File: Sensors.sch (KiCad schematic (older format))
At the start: 50 parts, among them CON1 CONSOLE, P1 CONN_02X20, P10 CBUS, P11 I2C0, P12 I2C0, P13 I2C1, P14 I2C1, P7 96B_SPI, Q2 CJ2305, Q3 CJ2305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

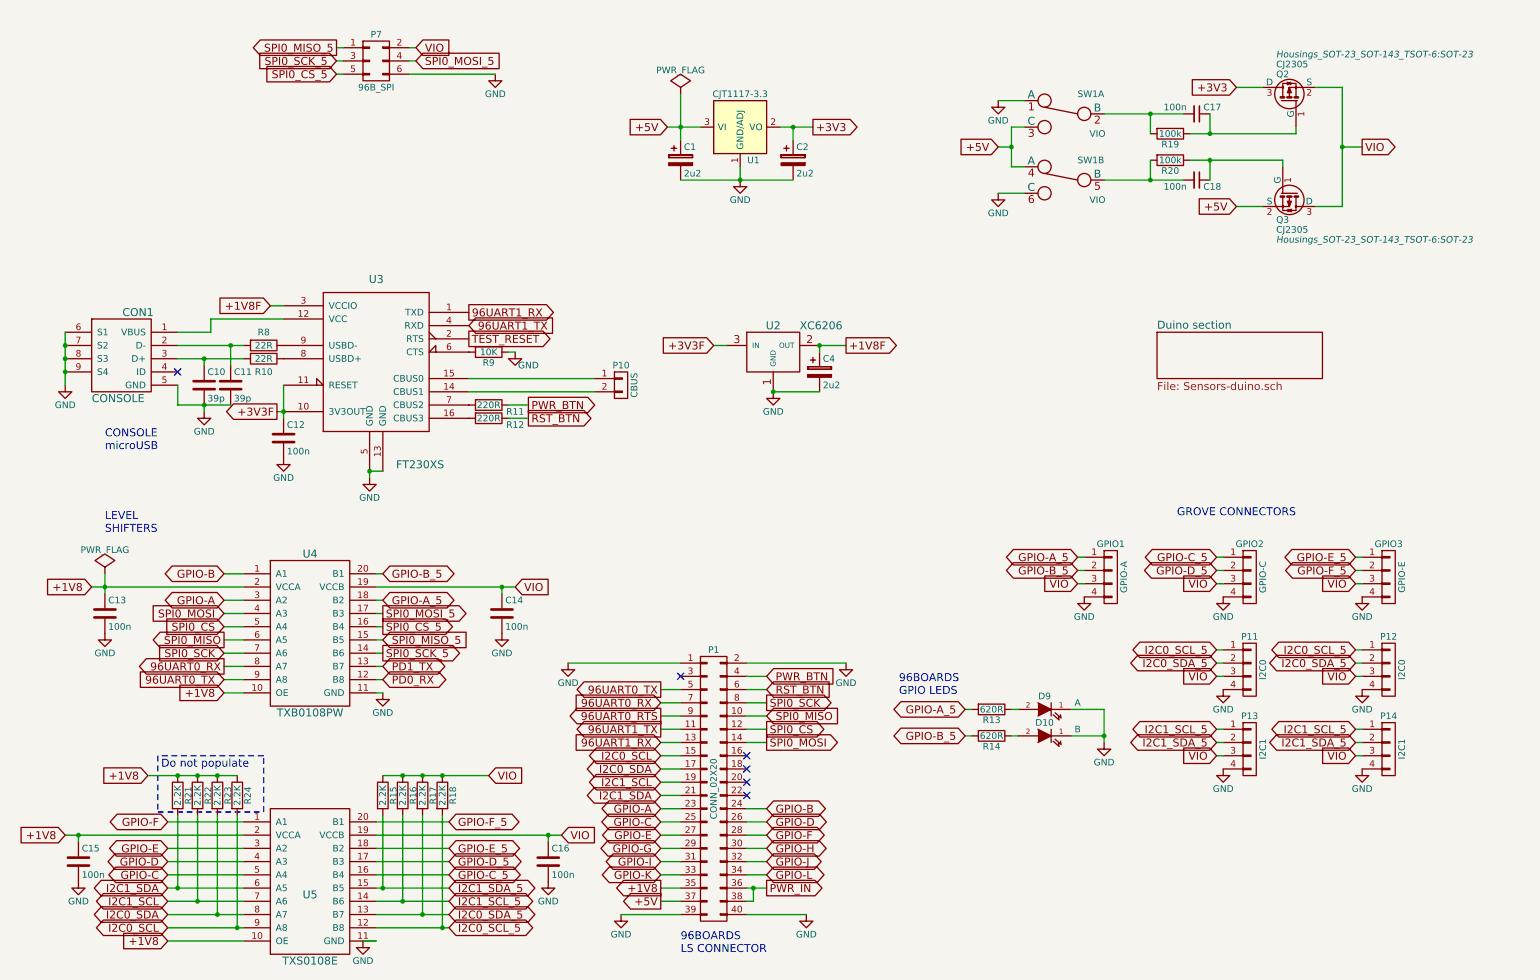
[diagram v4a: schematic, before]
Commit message: Fix DRC errors on schematic
Fix the following problems:
- Fix missing drive pin on VIO signal. Fixed by added PWR_FLAG component
- Unconnected labels on GPIO G-L. Fixed by removing labels and replacing
  with no-connect

Signed-off-by: Grant Likely <grant.likely@linaro.org>
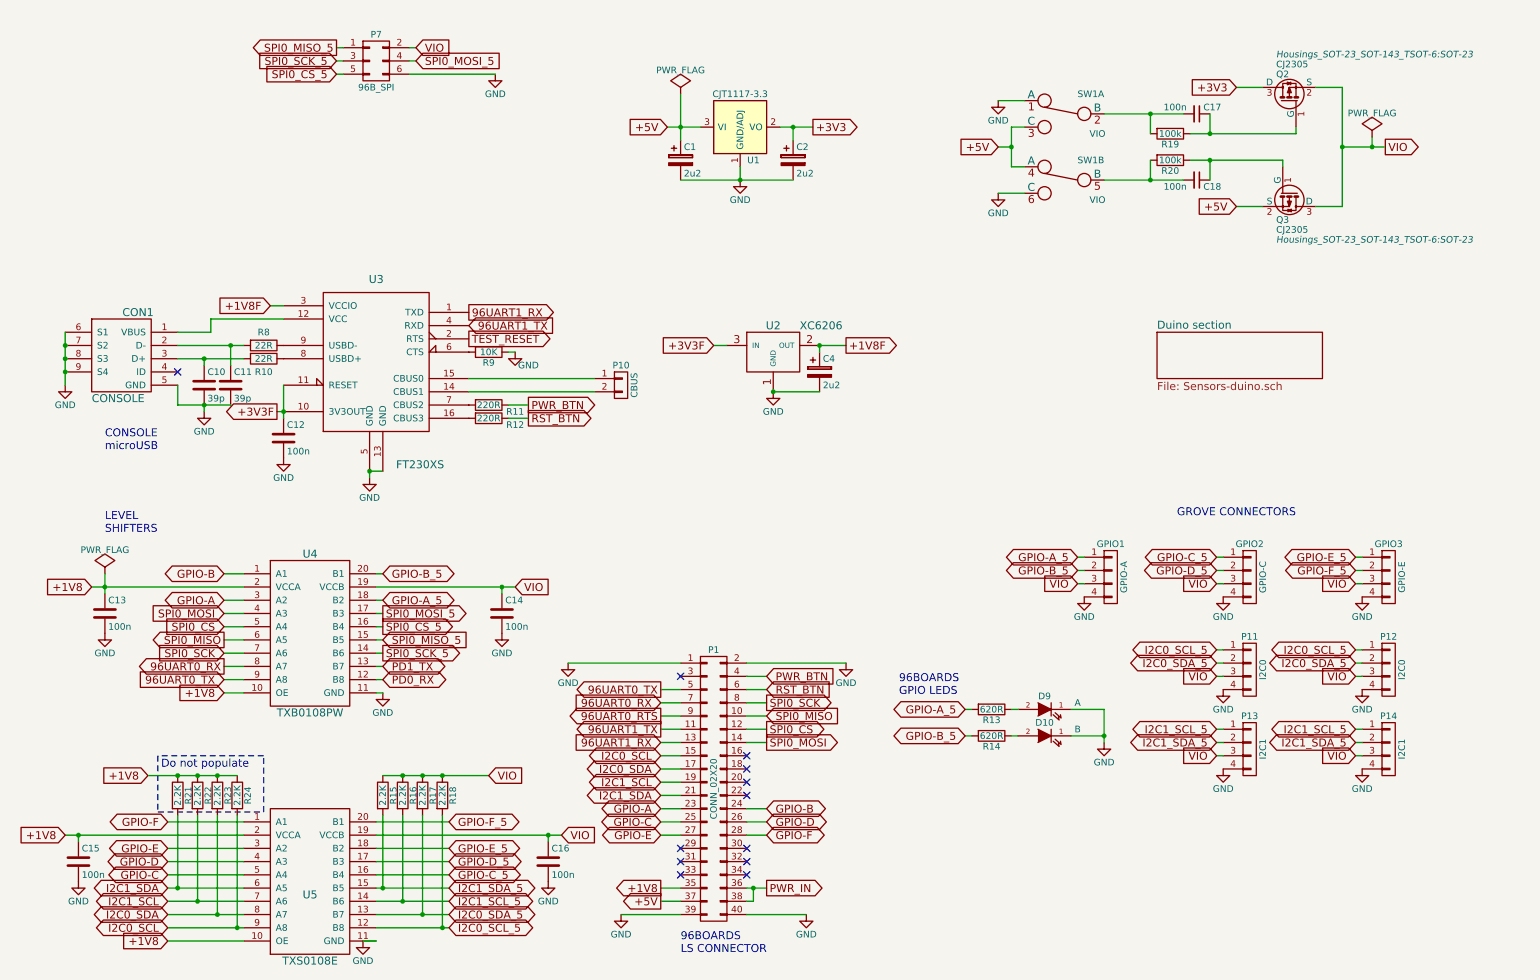
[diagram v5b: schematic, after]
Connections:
- net GPIO-G: no longer names the net of P1.29 (P29)
- net GPIO-H: no longer names the net of P1.30 (P30)
- net GPIO-I: no longer names the net of P1.31 (P31)
- net GPIO-J: no longer names the net of P1.32 (P32)
- net GPIO-K: no longer names the net of P1.33 (P33)
- net GPIO-L: no longer names the net of P1.34 (P34)
- no-connect marks 6 -> 12
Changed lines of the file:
@@
 $EndComp
 $Comp
-L GND #PWR18
+L GND #PWR01
 U 1 1 55BDFE9A
 P 9650 5700
-F 0 "#PWR18" H 9650 5450 50  0001 C CNN
+F 0 "#PWR01" H 9650 5450 50  0001 C CNN
 F 1 "GND" H 9650 5550 50  0000 C CNN
 F 2 "" H 9650 5700 60  0000 C CNN
@@
 $EndComp
 $Comp
-L GND #PWR19
+L GND #PWR02
 U 1 1 55BDFED8
 P 10700 5700
-F 0 "#PWR19" H 10700 5450 50  0001 C CNN
+F 0 "#PWR02" H 10700 5450 50  0001 C CNN
 F 1 "GND" H 10700 5550 50  0000 C CNN
 F 2 "" H 10700 5700 60  0000 C CNN
@@
 96UART0_TX
 $Comp
-L GND #PWR20
+L GND #PWR03
 U 1 1 55BE8D17
 P 3300 5725
-F 0 "#PWR20" H 3300 5475 50  0001 C CNN
+F 0 "#PWR03" H 3300 5475 50  0001 C CNN
 F 1 "GND" H 3300 5575 50  0000 C CNN
 F 2 "" H 3300 5725 60  0000 C CNN
@@
 $EndComp
 $Comp
-L GND #PWR15
+L GND #PWR04
 U 1 1 55BE99A8
 P 4200 5275
-F 0 "#PWR15" H 4200 5025 50  0001 C CNN
+F 0 "#PWR04" H 4200 5025 50  0001 C CNN
 F 1 "GND" H 4200 5125 50  0000 C CNN
 F 2 "" H 4200 5275 60  0000 C CNN
@@
 $EndComp
 $Comp
-L GND #PWR14
+L GND #PWR05
 U 1 1 55BE99F6
 P 1200 5275
-F 0 "#PWR14" H 1200 5025 50  0001 C CNN
+F 0 "#PWR05" H 1200 5025 50  0001 C CNN
 F 1 "GND" H 1200 5125 50  0000 C CNN
 F 2 "" H 1200 5275 60  0000 C CNN
@@
 $EndComp
 $Comp
-L GND #PWR17
+L GND #PWR06
 U 1 1 55BEA06E
 P 6800 5500
-F 0 "#PWR17" H 6800 5250 50  0001 C CNN
+F 0 "#PWR06" H 6800 5250 50  0001 C CNN
 F 1 "GND" H 6800 5350 50  0000 C CNN
 F 2 "" H 6800 5500 60  0000 C CNN
@@
 $EndComp
 $Comp
-L GND #PWR27
+L GND #PWR07
 U 1 1 55BEA0BC
 P 6500 7400
-F 0 "#PWR27" H 6500 7150 50  0001 C CNN
+F 0 "#PWR07" H 6500 7150 50  0001 C CNN
 F 1 "GND" H 6500 7250 50  0000 C CNN
 F 2 "" H 6500 7400 60  0000 C CNN
@@
 $EndComp
 $Comp
-L GND #PWR26
+L GND #PWR08
 U 1 1 55BEA10A
 P 5100 7400
-F 0 "#PWR26" H 5100 7150 50  0001 C CNN
+F 0 "#PWR08" H 5100 7150 50  0001 C CNN
 F 1 "GND" H 5100 7250 50  0000 C CNN
 F 2 "" H 5100 7400 60  0000 C CNN
@@
 96UART0_RX
 $Comp
-L GND #PWR16
+L GND #PWR09
 U 1 1 55BEAA68
 P 4700 5500
-F 0 "#PWR16" H 4700 5250 50  0001 C CNN
+F 0 "#PWR09" H 4700 5250 50  0001 C CNN
 F 1 "GND" H 4700 5350 50  0000 C CNN
 F 2 "" H 4700 5500 60  0000 C CNN
@@
 $EndComp
 $Comp
-L GND #PWR3
+L GND #PWR010
 U 1 1 55BEB06A
 P 6000 1850
-F 0 "#PWR3" H 6000 1600 50  0001 C CNN
+F 0 "#PWR010" H 6000 1600 50  0001 C CNN
 F 1 "GND" H 6000 1700 50  0000 C CNN
 F 2 "" H 6000 1850 60  0000 C CNN
@@
 $EndComp
 $Comp
-L GND #PWR24
+L GND #PWR011
 U 1 1 55C520B5
 P 1000 7150
-F 0 "#PWR24" H 1000 6900 50  0001 C CNN
+F 0 "#PWR011" H 1000 6900 50  0001 C CNN
 F 1 "GND" H 1000 7000 50  0000 C CNN
 F 2 "" H 1000 7150 60  0000 C CNN
@@
 $EndComp
 $Comp
-L GND #PWR28
+L GND #PWR012
 U 1 1 55C52215
 P 3150 7600
-F 0 "#PWR28" H 3150 7350 50  0001 C CNN
+F 0 "#PWR012" H 3150 7350 50  0001 C CNN
 F 1 "GND" H 3150 7450 50  0000 C CNN
 F 2 "" H 3150 7600 60  0000 C CNN
@@
 $EndComp
 $Comp
-L GND #PWR25
+L GND #PWR013
 U 1 1 55C5257D
 P 4550 7150
-F 0 "#PWR25" H 4550 6900 50  0001 C CNN
+F 0 "#PWR013" H 4550 6900 50  0001 C CNN
 F 1 "GND" H 4550 7000 50  0000 C CNN
 F 2 "" H 4550 7150 60  0000 C CNN
@@
 $EndComp
 $Comp
-L GND #PWR21
+L GND #PWR014
 U 1 1 55C55EA3
 P 8750 6100
-F 0 "#PWR21" H 8750 5850 50  0001 C CNN
+F 0 "#PWR014" H 8750 5850 50  0001 C CNN
 F 1 "GND" H 8750 5950 50  0000 C CNN
 F 2 "" H 8750 6100 60  0000 C CNN
@@
 $EndComp
 $Comp
-L GND #PWR6
+L GND #PWR015
 U 1 1 55C61734
 P 900 3400
-F 0 "#PWR6" H 900 3150 50  0001 C CNN
+F 0 "#PWR015" H 900 3150 50  0001 C CNN
 F 1 "GND" H 900 3250 50  0000 C CNN
 F 2 "" H 900 3400 60  0000 C CNN
@@
 $EndComp
 $Comp
-L GND #PWR8
+L GND #PWR016
 U 1 1 55C6244A
 P 1950 3600
-F 0 "#PWR8" H 1950 3350 50  0001 C CNN
+F 0 "#PWR016" H 1950 3350 50  0001 C CNN
 F 1 "GND" H 1950 3450 50  0000 C CNN
 F 2 "" H 1950 3600 60  0000 C CNN
@@
 $EndComp
 $Comp
-L GND #PWR9
+L GND #PWR017
 U 1 1 55C62C95
 P 2550 3950
-F 0 "#PWR9" H 2550 3700 50  0001 C CNN
+F 0 "#PWR017" H 2550 3700 50  0001 C CNN
 F 1 "GND" H 2550 3800 50  0000 C CNN
 F 2 "" H 2550 3950 60  0000 C CNN
@@
 $EndComp
 $Comp
-L GND #PWR10
+L GND #PWR018
 U 1 1 55C6311C
 P 3200 4100
-F 0 "#PWR10" H 3200 3850 50  0001 C CNN
+F 0 "#PWR018" H 3200 3850 50  0001 C CNN
 F 1 "GND" H 3200 3950 50  0000 C CNN
 F 2 "" H 3200 4100 60  0000 C CNN
@@
 $EndComp
 $Comp
-L GND #PWR5
+L GND #PWR019
 U 1 1 55C634DE
 P 4300 3150
-F 0 "#PWR5" H 4300 2900 50  0001 C CNN
+F 0 "#PWR019" H 4300 2900 50  0001 C CNN
 F 1 "GND" H 4400 3050 50  0000 C CNN
 F 2 "" H 4300 3150 60  0000 C CNN
@@
 $EndComp
 $Comp
-L GND #PWR7
+L GND #PWR020
 U 1 1 55CBD558
 P 6250 3450
-F 0 "#PWR7" H 6250 3200 50  0001 C CNN
+F 0 "#PWR020" H 6250 3200 50  0001 C CNN
 F 1 "GND" H 6250 3300 50  0000 C CNN
 F 2 "" H 6250 3450 60  0000 C CNN
@@
 +1V8
 $Comp
-L PWR_FLAG #FLG2
+L PWR_FLAG #FLG021
 U 1 1 55CD081A
 P 1200 4825
-F 0 "#FLG2" H 1200 4920 50  0001 C CNN
+F 0 "#FLG021" H 1200 4920 50  0001 C CNN
 F 1 "PWR_FLAG" H 1200 5005 50  0000 C CNN
 F 2 "" H 1200 4825 60  0000 C CNN
@@
 Text GLabel 6200 6800 2    60   BiDi ~ 0
 GPIO-F
-Text GLabel 6200 6900 2    60   BiDi ~ 0
-GPIO-H
-Text GLabel 6200 7000 2    60   BiDi ~ 0
-GPIO-J
-Text GLabel 6200 7100 2    60   BiDi ~ 0
-GPIO-L
 Text GLabel 5400 6800 0    60   BiDi ~ 0
 GPIO-E
-Text GLabel 5400 6900 0    60   BiDi ~ 0
-GPIO-G
-Text GLabel 5400 7000 0    60   BiDi ~ 0
-GPIO-I
-Text GLabel 5400 7100 0    60   BiDi ~ 0
-GPIO-K
 Text GLabel 2100 5425 0    60   Input ~ 0
 SPI0_SCK
@@
 $EndComp
 $Comp
-L GND #PWR13
+L GND #PWR022
 U 1 1 5616B62D
 P 10700 5000
-F 0 "#PWR13" H 10700 4750 50  0001 C CNN
+F 0 "#PWR022" H 10700 4750 50  0001 C CNN
 F 1 "GND" H 10700 4850 50  0000 C CNN
 F 2 "" H 10700 5000 60  0000 C CNN
@@
 SPI0_CS_5
 $Comp
-L GND #PWR1
+L GND #PWR023
 U 1 1 5616A1D1
 P 4150 1050
-F 0 "#PWR1" H 4150 800 50  0001 C CNN
+F 0 "#PWR023" H 4150 800 50  0001 C CNN
 F 1 "GND" H 4150 900 50  0000 C CNN
 F 2 "" H 4150 1050 60  0000 C CNN
@@
 VIO
 $Comp
-L GND #PWR12
+L GND #PWR024
 U 1 1 55C535E8
 P 9650 5000
-F 0 "#PWR12" H 9650 4750 50  0001 C CNN
+F 0 "#PWR024" H 9650 4750 50  0001 C CNN
 F 1 "GND" H 9650 4850 50  0000 C CNN
 F 2 "" H 9650 5000 60  0000 C CNN
@@
 VIO
 $Comp
-L GND #PWR11
+L GND #PWR025
 U 1 1 561DB32B
 P 8600 5000
-F 0 "#PWR11" H 8600 4750 50  0001 C CNN
+F 0 "#PWR025" H 8600 4750 50  0001 C CNN
 F 1 "GND" H 8600 4850 50  0000 C CNN
 F 2 "" H 8600 5000 60  0000 C CNN
@@
 $EndComp
 $Comp
-L GND #PWR22
+L GND #PWR026
 U 1 1 561DD720
 P 9650 6300
-F 0 "#PWR22" H 9650 6050 50  0001 C CNN
+F 0 "#PWR026" H 9650 6050 50  0001 C CNN
 F 1 "GND" H 9650 6150 50  0000 C CNN
 F 2 "" H 9650 6300 60  0000 C CNN
@@
 $EndComp
 $Comp
-L GND #PWR23
+L GND #PWR027
 U 1 1 5620C942
 P 10700 6300
-F 0 "#PWR23" H 10700 6050 50  0001 C CNN
+F 0 "#PWR027" H 10700 6050 50  0001 C CNN
 F 1 "GND" H 10700 6150 50  0000 C CNN
 F 2 "" H 10700 6300 60  0000 C CNN
@@
 $EndComp
 $Comp
-L GND #PWR2
+L GND #PWR028
 U 1 1 562DCAE3
 P 7950 1250
-F 0 "#PWR2" H 7950 1000 50  0001 C CNN
+F 0 "#PWR028" H 7950 1000 50  0001 C CNN
 F 1 "GND" H 7950 1100 50  0000 C CNN
 F 2 "" H 7950 1250 60  0000 C CNN
@@
 $EndComp
 $Comp
-L GND #PWR4
+L GND #PWR029
 U 1 1 562DCC2D
 P 7950 1950
-F 0 "#PWR4" H 7950 1700 50  0001 C CNN
+F 0 "#PWR029" H 7950 1700 50  0001 C CNN
 F 1 "GND" H 7950 1800 50  0000 C CNN
 F 2 "" H 7950 1950 60  0000 C CNN
@@
 	0    1    1    0
 $EndComp
-Text GLabel 10700 1600 2    60   Output ~ 0
+Text GLabel 10875 1600 2    60   Output ~ 0
 VIO
 Text GLabel 7950 1600 0    60   Input ~ 0
@@
 	1675 7600 2250 7600
 Wire Wire Line
-	5400 7100 5550 7100
-Wire Wire Line
-	5400 7000 5550 7000
-Wire Wire Line
-	5400 6900 5550 6900
-Wire Wire Line
 	5400 6800 5550 6800
-Wire Wire Line
-	6050 7100 6200 7100
-Wire Wire Line
-	6050 7000 6200 7000
-Wire Wire Line
-	6050 6900 6200 6900
 Wire Wire Line
 	6050 6800 6200 6800
@@
 Connection ~ 6400 1450
 Wire Wire Line
-	6400 1550 6400 1450
+	6400 1450 6400 1550
 Wire Wire Line
 	5550 1850 6400 1850
@@
 	10550 1150 10550 2050
 Wire Wire Line
-	10550 1600 10700 1600
+	10550 1600 10875 1600
 Wire Wire Line
 	10550 2050 10350 2050
@@
 +5V
 $Comp
-L PWR_FLAG #FLG1
+L PWR_FLAG #FLG030
 U 1 1 55C65C3C
 P 5550 1200
-F 0 "#FLG1" H 5550 1295 50  0001 C CNN
+F 0 "#FLG030" H 5550 1295 50  0001 C CNN
 F 1 "PWR_FLAG" H 5550 1380 50  0000 C CNN
 F 2 "" H 5550 1200 60  0000 C CNN
@@
 Wire Notes Line
 	1600 6200 1600 6625
+$Comp
+L PWR_FLAG #FLG031
+U 1 1 562FB62D
+P 10775 1525
+F 0 "#FLG031" H 10775 1620 50  0001 C CNN
+F 1 "PWR_FLAG" H 10775 1705 50  0000 C CNN
+F 2 "" H 10775 1525 60  0000 C CNN
+F 3 "" H 10775 1525 60  0000 C CNN
+	1    10775 1525
+	1    0    0    -1
+$EndComp
+NoConn ~ 6050 6900
+NoConn ~ 6050 7000
+NoConn ~ 6050 7100
+NoConn ~ 5550 6900
+NoConn ~ 5550 7000
+NoConn ~ 5550 7100
+Wire Wire Line
+	10775 1525 10775 1600
+Connection ~ 10775 1600
 $EndSCHEMATC

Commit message: Update the Seeed part numbers for generating the BOM
Signed-off-by: Grant Likely <grant.likely@linaro.org>
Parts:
- GPIO1, P11: Mfr Part # (none) -> 1125R-SMT-4P; Seeed SKU 320110033 -> 320110032
- GPIO2, GPIO3, P12, P13, P14: Mfr Part # (none) -> 1125S-4P
- P1: Mfr Part # P220-1220A0XMXXXX2 -> F243-1220xxxSUx1
- Q2, Q3: Mfr (none) -> JCET; Mfr Part # (none) -> CJ2305; Seeed SKU (none) -> 305030014
- R15, R16, R17, R18, R21, R22, R23, R24: Mfr (none) -> YAGEO; Mfr Part # (none) -> RC0603JR-072K2L; Seeed SKU (none) -> 301010124
- R19, R20: Mfr (none) -> YAGEO; Mfr Part # (none) -> RC0603FR-07100KL; Seeed SKU (none) -> 301010196
- SW1: Mfr (none) -> Deyilong; Mfr Part # (none) -> MS-22D18 G2; Seeed SKU (none) -> 311010004
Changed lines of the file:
@@
 F 3 "" H 5800 5500 60  0000 C CNN
 F 4 "Yxcon" H 2450 850 60  0001 C CNN "Mfr"
-F 5 "P220-1220A0XMXXXX2" H 2450 850 60  0001 C CNN "Mfr Part #"
+F 5 "F243-1220xxxSUx1" H 5800 6450 60  0001 C CNN "Mfr Part #"
 	1    5800 6450
 	1    0    0    -1
@@
 F 2 "Sensors:Grove_SMD_Connector" H 9850 5550 60  0001 C CNN
 F 3 "" H 9850 5550 60  0000 C CNN
-F 4 "320110033" H 2500 400 60  0001 C CNN "Seeed SKU"
+F 4 "320110032" H 2500 400 60  0001 C CNN "Seeed SKU"
 F 5 "Taifeng" H 2500 400 60  0001 C CNN "Mfr"
+F 6 "1125R-SMT-4P" H 9850 5550 60  0001 C CNN "Mfr Part #"
 	1    9850 5550
 	1    0    0    -1
@@
 F 4 "320110033" H 2450 400 60  0001 C CNN "Seeed SKU"
 F 5 "Taifeng" H 2450 400 60  0001 C CNN "Mfr"
+F 6 "1125S-4P" H 10900 5550 60  0001 C CNN "Mfr Part #"
 	1    10900 5550
 	1    0    0    -1
@@
 F 2 "Sensors:R_0603_Seeed" V 3230 6500 30  0001 C CNN
 F 3 "" H 3300 6500 30  0000 C CNN
+F 4 "301010124" H 3300 6500 60  0001 C CNN "Seeed SKU"
+F 5 "YAGEO" H 3300 6500 60  0001 C CNN "Mfr"
+F 6 "RC0603JR-072K2L" H 3300 6500 60  0001 C CNN "Mfr Part #"
 	1    3300 6500
 	1    0    0    -1
@@
 F 2 "Sensors:R_0603_Seeed" V 3380 6500 30  0001 C CNN
 F 3 "" H 3450 6500 30  0000 C CNN
+F 4 "301010124" H 3450 6500 60  0001 C CNN "Seeed SKU"
+F 5 "YAGEO" H 3450 6500 60  0001 C CNN "Mfr"
+F 6 "RC0603JR-072K2L" H 3450 6500 60  0001 C CNN "Mfr Part #"
 	1    3450 6500
 	1    0    0    -1
@@
 F 2 "Sensors:R_0603_Seeed" V 3530 6500 30  0001 C CNN
 F 3 "" H 3600 6500 30  0000 C CNN
+F 4 "301010124" H 3600 6500 60  0001 C CNN "Seeed SKU"
+F 5 "YAGEO" H 3600 6500 60  0001 C CNN "Mfr"
+F 6 "RC0603JR-072K2L" H 3600 6500 60  0001 C CNN "Mfr Part #"
 	1    3600 6500
 	1    0    0    -1
@@
 F 2 "Sensors:R_0603_Seeed" V 3680 6500 30  0001 C CNN
 F 3 "" H 3750 6500 30  0000 C CNN
+F 4 "301010124" H 3750 6500 60  0001 C CNN "Seeed SKU"
+F 5 "YAGEO" H 3750 6500 60  0001 C CNN "Mfr"
+F 6 "RC0603JR-072K2L" H 3750 6500 60  0001 C CNN "Mfr Part #"
 	1    3750 6500
 	1    0    0    -1
@@
 F 4 "320110033" H 2450 450 60  0001 C CNN "Seeed SKU"
 F 5 "Taifeng" H 2450 450 60  0001 C CNN "Mfr"
+F 6 "1125S-4P" H 10900 4850 60  0001 C CNN "Mfr Part #"
 	1    10900 4850
 	1    0    0    -1
@@
 F 4 "320110033" H 1400 450 60  0001 C CNN "Seeed SKU"
 F 5 "Taifeng" H 1400 450 60  0001 C CNN "Mfr"
+F 6 "1125S-4P" H 9850 4850 60  0001 C CNN "Mfr Part #"
 	1    9850 4850
 	1    0    0    -1
@@
 F 2 "Sensors:Grove_SMD_Connector" H 8800 4850 60  0001 C CNN
 F 3 "" H 8800 4850 60  0000 C CNN
-F 4 "320110033" H 350 450 60  0001 C CNN "Seeed SKU"
+F 4 "320110032" H 350 450 60  0001 C CNN "Seeed SKU"
 F 5 "Taifeng" H 350 450 60  0001 C CNN "Mfr"
+F 6 "1125R-SMT-4P" H 8800 4850 60  0001 C CNN "Mfr Part #"
 	1    8800 4850
 	1    0    0    -1
@@
 F 4 "320110033" H 1400 1000 60  0001 C CNN "Seeed SKU"
 F 5 "Taifeng" H 1400 1000 60  0001 C CNN "Mfr"
+F 6 "1125S-4P" H 9850 6150 60  0001 C CNN "Mfr Part #"
 	1    9850 6150
 	1    0    0    -1
@@
 F 4 "320110033" H 2450 1000 60  0001 C CNN "Seeed SKU"
 F 5 "Taifeng" H 2450 1000 60  0001 C CNN "Mfr"
+F 6 "1125S-4P" H 10900 6150 60  0001 C CNN "Mfr Part #"
 	1    10900 6150
 	1    0    0    -1
@@
 F 2 "Housings_SOT-23_SOT-143_TSOT-6:SOT-23" V 10500 1350 50  0000 R CIN
 F 3 "" H 10150 1250 50  0000 L CNN
+F 4 "305030014" H 10150 1250 60  0001 C CNN "Seeed SKU"
+F 5 "JCET" H 10150 1250 60  0001 C CNN "Mfr"
+F 6 "CJ2305" H 10150 1250 60  0001 C CNN "Mfr Part #"
 	1    10150 1250
 	0    -1   -1   0
@@
 F 2 "Sensors:DIP_Toggle_Switch" H 8450 1350 60  0001 C CNN
 F 3 "" H 8450 1350 60  0000 C CNN
+F 4 "311010004" H 8450 1350 60  0001 C CNN "Seeed SKU"
+F 5 "Deyilong" H 8450 1350 60  0001 C CNN "Mfr"
+F 6 "MS-22D18 G2" H 8450 1350 60  0001 C CNN "Mfr Part #"
 	1    8450 1350
 	-1   0    0    -1
@@
 F 2 "Sensors:R_0603_Seeed" V 9180 1500 30  0001 C CNN
 F 3 "" H 9250 1500 30  0000 C CNN
+F 4 "301010196" H 9250 1500 60  0001 C CNN "Seeed SKU"
+F 5 "YAGEO" H 9250 1500 60  0001 C CNN "Mfr"
+F 6 "RC0603FR-07100KL" H 9250 1500 60  0001 C CNN "Mfr Part #"
 	1    9250 1500
 	0    1    1    0
@@
 F 2 "Sensors:R_0603_Seeed" V 9180 1700 30  0001 C CNN
 F 3 "" H 9250 1700 30  0000 C CNN
+F 4 "301010196" H 9250 1700 60  0001 C CNN "Seeed SKU"
+F 5 "YAGEO" H 9250 1700 60  0001 C CNN "Mfr"
+F 6 "RC0603FR-07100KL" H 9250 1700 60  0001 C CNN "Mfr Part #"
 	1    9250 1700
 	0    1    1    0
@@
 F 2 "Housings_SOT-23_SOT-143_TSOT-6:SOT-23" V 10500 1850 50  0000 L CIN
 F 3 "" H 10150 1950 50  0000 L CNN
+F 4 "305030014" H 10150 1950 60  0001 C CNN "Seeed SKU"
+F 5 "JCET" H 10150 1950 60  0001 C CNN "Mfr"
+F 6 "CJ2305" H 10150 1950 60  0001 C CNN "Mfr Part #"
 	1    10150 1950
 	0    1    1    0
@@
 F 2 "Sensors:R_0603_Seeed" V 1680 6500 30  0001 C CNN
 F 3 "" H 1750 6500 30  0000 C CNN
+F 4 "301010124" H 1750 6500 60  0001 C CNN "Seeed SKU"
+F 5 "YAGEO" H 1750 6500 60  0001 C CNN "Mfr"
+F 6 "RC0603JR-072K2L" H 1750 6500 60  0001 C CNN "Mfr Part #"
 	1    1750 6500
 	1    0    0    -1
@@
 F 2 "Sensors:R_0603_Seeed" V 1830 6500 30  0001 C CNN
 F 3 "" H 1900 6500 30  0000 C CNN
+F 4 "301010124" H 1900 6500 60  0001 C CNN "Seeed SKU"
+F 5 "YAGEO" H 1900 6500 60  0001 C CNN "Mfr"
+F 6 "RC0603JR-072K2L" H 1900 6500 60  0001 C CNN "Mfr Part #"
 	1    1900 6500
 	1    0    0    -1
@@
 F 2 "Sensors:R_0603_Seeed" V 1980 6500 30  0001 C CNN
 F 3 "" H 2050 6500 30  0000 C CNN
+F 4 "301010124" H 2050 6500 60  0001 C CNN "Seeed SKU"
+F 5 "YAGEO" H 2050 6500 60  0001 C CNN "Mfr"
+F 6 "RC0603JR-072K2L" H 2050 6500 60  0001 C CNN "Mfr Part #"
 	1    2050 6500
 	1    0    0    -1
@@
 F 2 "Sensors:R_0603_Seeed" V 2130 6500 30  0001 C CNN
 F 3 "" H 2200 6500 30  0000 C CNN
+F 4 "301010124" H 2200 6500 60  0001 C CNN "Seeed SKU"
+F 5 "YAGEO" H 2200 6500 60  0001 C CNN "Mfr"
+F 6 "RC0603JR-072K2L" H 2200 6500 60  0001 C CNN "Mfr Part #"
 	1    2200 6500
 	1    0    0    -1
